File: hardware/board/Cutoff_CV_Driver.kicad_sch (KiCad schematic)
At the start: 18 parts

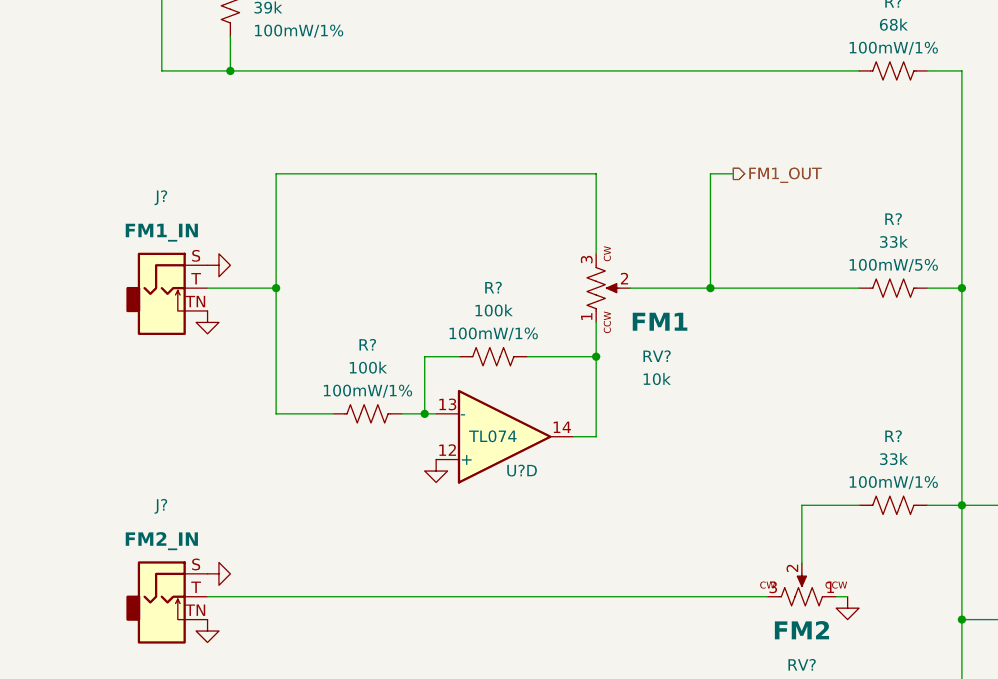
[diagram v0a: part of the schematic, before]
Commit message: Updated Schematic
-Added R935, R936, and Q901 to make resonance self oscillation LED turn on sharply

-Moved D929, D930, and added R933, R934 to make FM1 LED more sensitive

-Changed FM1 Attenuverter and added R410 and R411 to make FM1 Knob have some curve/deadzone

-Changed Resonance VCA output and added R623 and R624 to make resonance VCA output higher voltage to avoid opamp offset being significant .

-Added testing documents
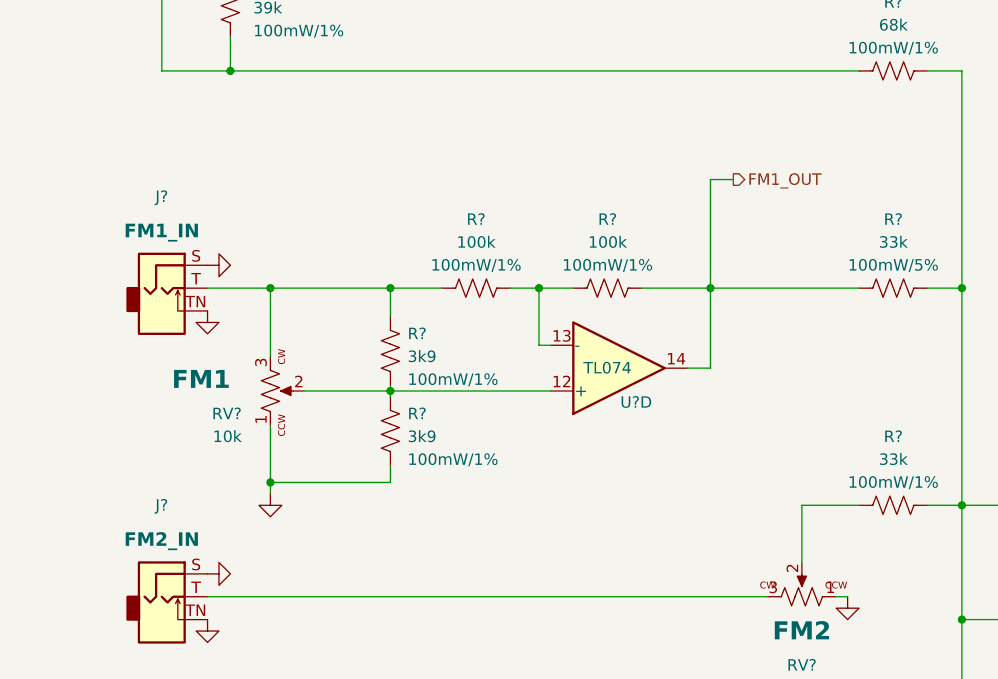
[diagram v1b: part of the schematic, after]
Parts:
- added R? (x2): 3k9, winterbloom:R_0603_HandSolder, symbol Device:R_US
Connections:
- net FM1_OUT: now also R?.1, U?.14; no longer RV?.2
- net GND: now also RV?.1, R?.2; no longer U?.12 (+)
- net at J?.T (Tip), R?.2, RV?.3: now also R?.1
- new net: R?.1, R?.2, RV?.2, U?.12 (+)
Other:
- moved on the sheet: R?, RV?, U?D

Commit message: Updated PCB to add and routed new components.
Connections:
- net INSTABILITY_IN renamed SALT_IN
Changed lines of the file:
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@@
   (title_block
     (title "Neptune")
-    (date "2023-07-20")
+    (date "2023-09-26")
     (rev "v0")
     (company "Winterbloom")
@@
     (effects (font (size 1.27 1.27)) (justify left))
   )
-  (hierarchical_label "INSTABILITY_IN" (shape input) (at 104.14 152.4 180) (fields_autoplaced)
+  (hierarchical_label "SALT_IN" (shape input) (at 104.14 152.4 180) (fields_autoplaced)
     (effects (font (size 1.27 1.27)) (justify right))
   )

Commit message: Lots of various small changes after reviewing the checklist.
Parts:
- R?: Rating 100mW/5% -> 100mW/1%
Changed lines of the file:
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@@
   (title_block
     (title "Neptune")
-    (date "2023-09-26")
-    (rev "v0")
+    (date "2023-10-10")
+    (rev "v1")
     (company "Winterbloom")
     (comment 1 "Carson Walls")
@@
       (effects (font (size 1.27 1.27)) hide)
     )
-    (property "Rating" "100mW/5%" (at 177.8 96.52 90)
-      (effects (font (size 1.27 1.27)))
-    )
+    (property "Rating" "100mW/1%" (at 177.8 96.52 90)
+      (effects (font (size 1.27 1.27)))
+    )

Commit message: hardware: add MPNs, DigiKey part numbers, and LCSC part numbers for all BOM items
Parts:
- C?: DigiKey (none) -> 1276-1008-1-ND; LCSC (none) -> C14858; MPN (none) -> CL10C101JB8NNNC; Rating 25V/10% -> 25V/10%/C0G; Substitutes Allowed (none) -> Yes
- R? (x2): DigiKey (none) -> 13-RT0603FRE13100KLTR-ND; LCSC (none) -> C4107493; MPN (none) -> RT0603FRE13100KL; Rating 100mW/1% -> 100mW/1%/Thin; Substitutes Allowed (none) -> Yes
- R? (x3): DigiKey (none) -> YAG5961CT-ND; LCSC (none) -> C863790; MPN (none) -> RT0603FRE073K9L; Rating 100mW/1% -> 100mW/1%/Thin; Substitutes Allowed (none) -> Yes
- R? (x2): DigiKey (none) -> YAG5967CT-ND; LCSC (none) -> C706189; MPN (none) -> RT0603FRE0768KL; Rating 100mW/1% -> 100mW/1%/Thin; Substitutes Allowed (none) -> Yes
- R?: DigiKey (none) -> YAG2321CT-ND; LCSC (none) -> C469659; MPN (none) -> RT0603FRE0710KL; Rating 100mW/1% -> 100mW/1%/Thin; Substitutes Allowed (none) -> Yes
- R? (x2): DigiKey (none) -> YAG5959CT-ND; LCSC (none) -> C706162; MPN (none) -> RT0603FRE0733KL; Rating 100mW/1% -> 100mW/1%/Thin; Substitutes Allowed (none) -> Yes
- R?: DigiKey (none) -> 13-RT0603FRE0739KLCT-ND; LCSC (none) -> C706166; MPN (none) -> RT0603FRE0739KL; Rating 100mW/1% -> 100mW/1%/Thin; Substitutes Allowed (none) -> Yes
- U? (x2): DigiKey (none) -> 296-7198-1-ND; LCSC (none) -> C96507; MPN TL074CPW -> TL074CPWR; Substitutes Allowed (none) -> No

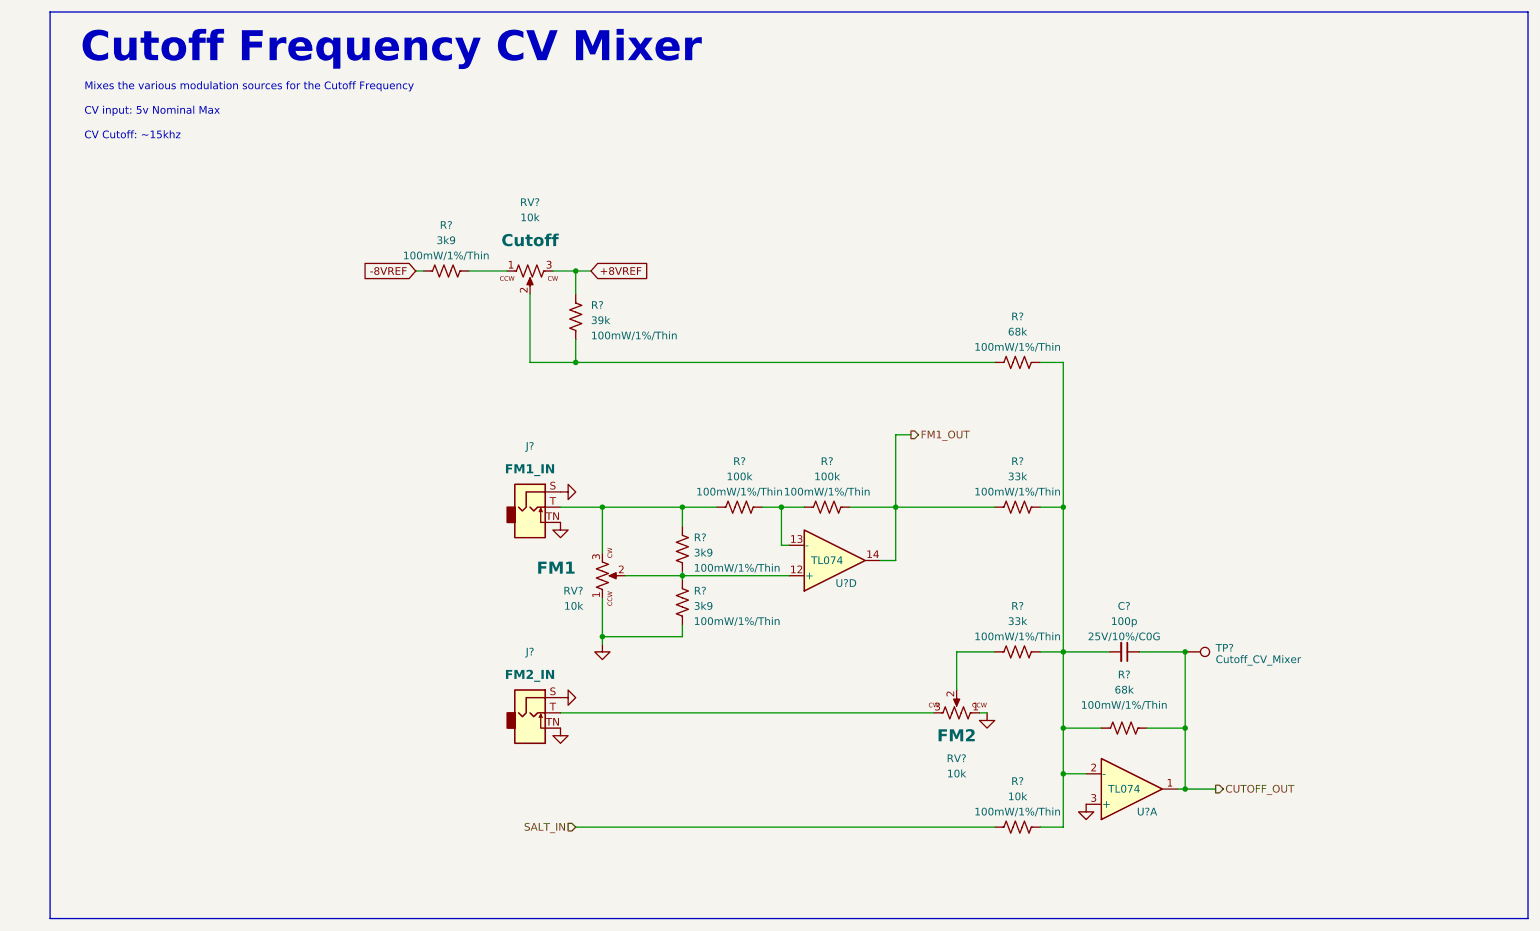
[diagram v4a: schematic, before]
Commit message: hardware: update schematic fonts/text sizes, some slight readability improvements
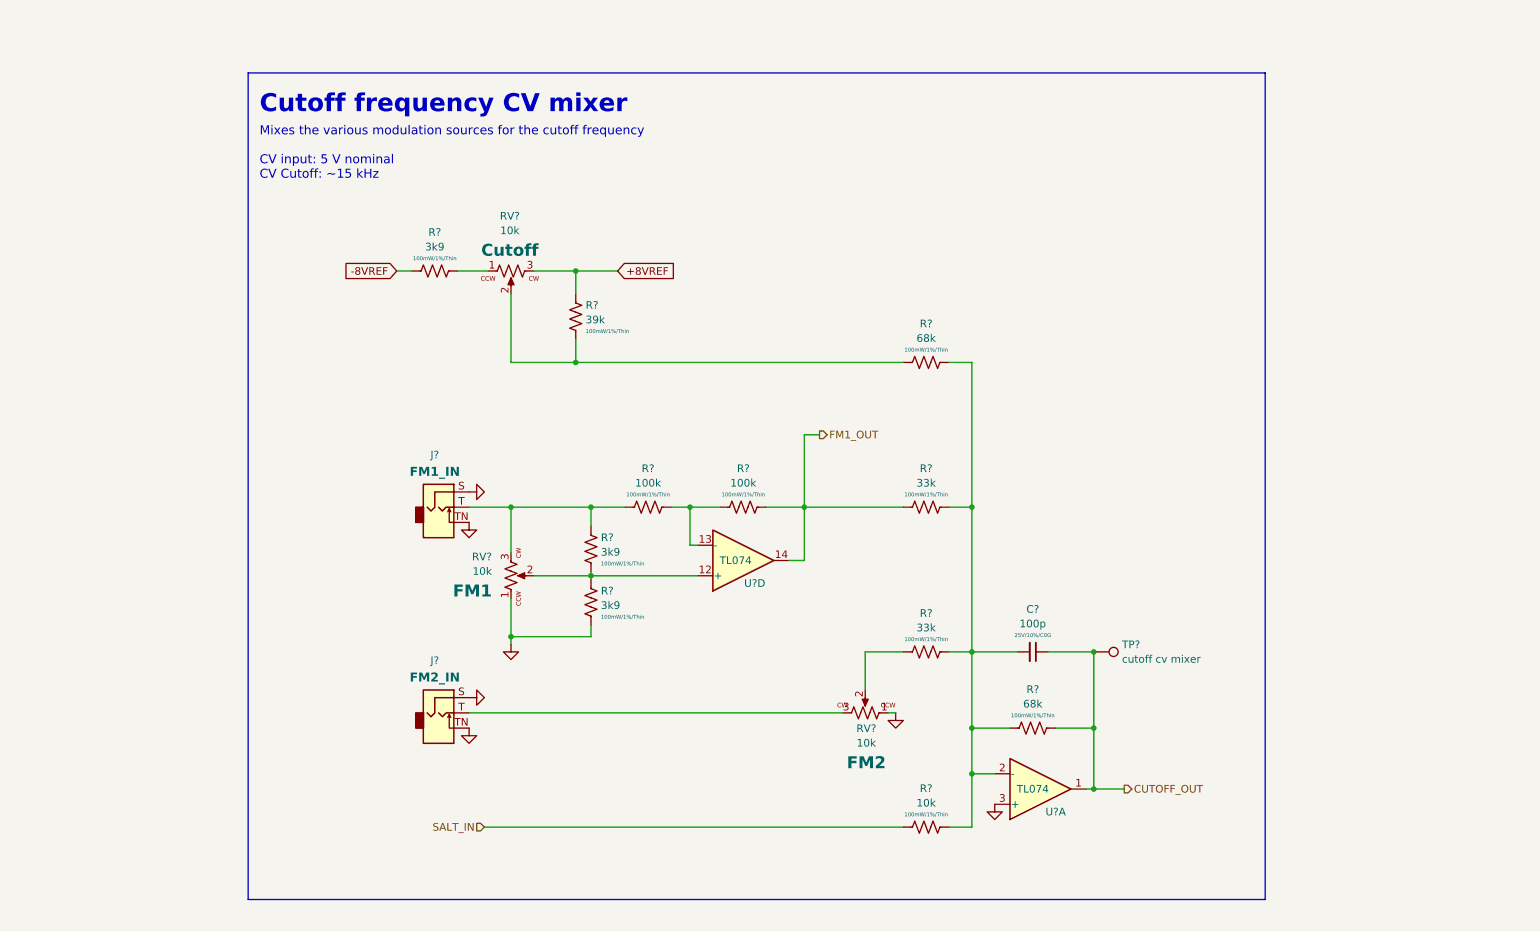
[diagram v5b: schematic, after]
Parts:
- TP?: Name Cutoff_CV_Mixer -> cutoff cv mixer
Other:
- note added: "Cutoff frequency CV mixer"
- note added: "Mixes the various modulation sources for the cutoff frequency CV input: 5 V nominal CV Cutoff: ~15 kHz"
- note removed: "Cutoff Frequency CV Mixer"
- note removed: "Mixes the various modulation sources for the Cutoff Frequency CV input: 5v Nominal Max CV Cutoff: ~15khz"
- moved on the sheet: C?, J?, R?, RV?, TP?, U?A, U?D

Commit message: hardware: use new Winterbloom sheet layout
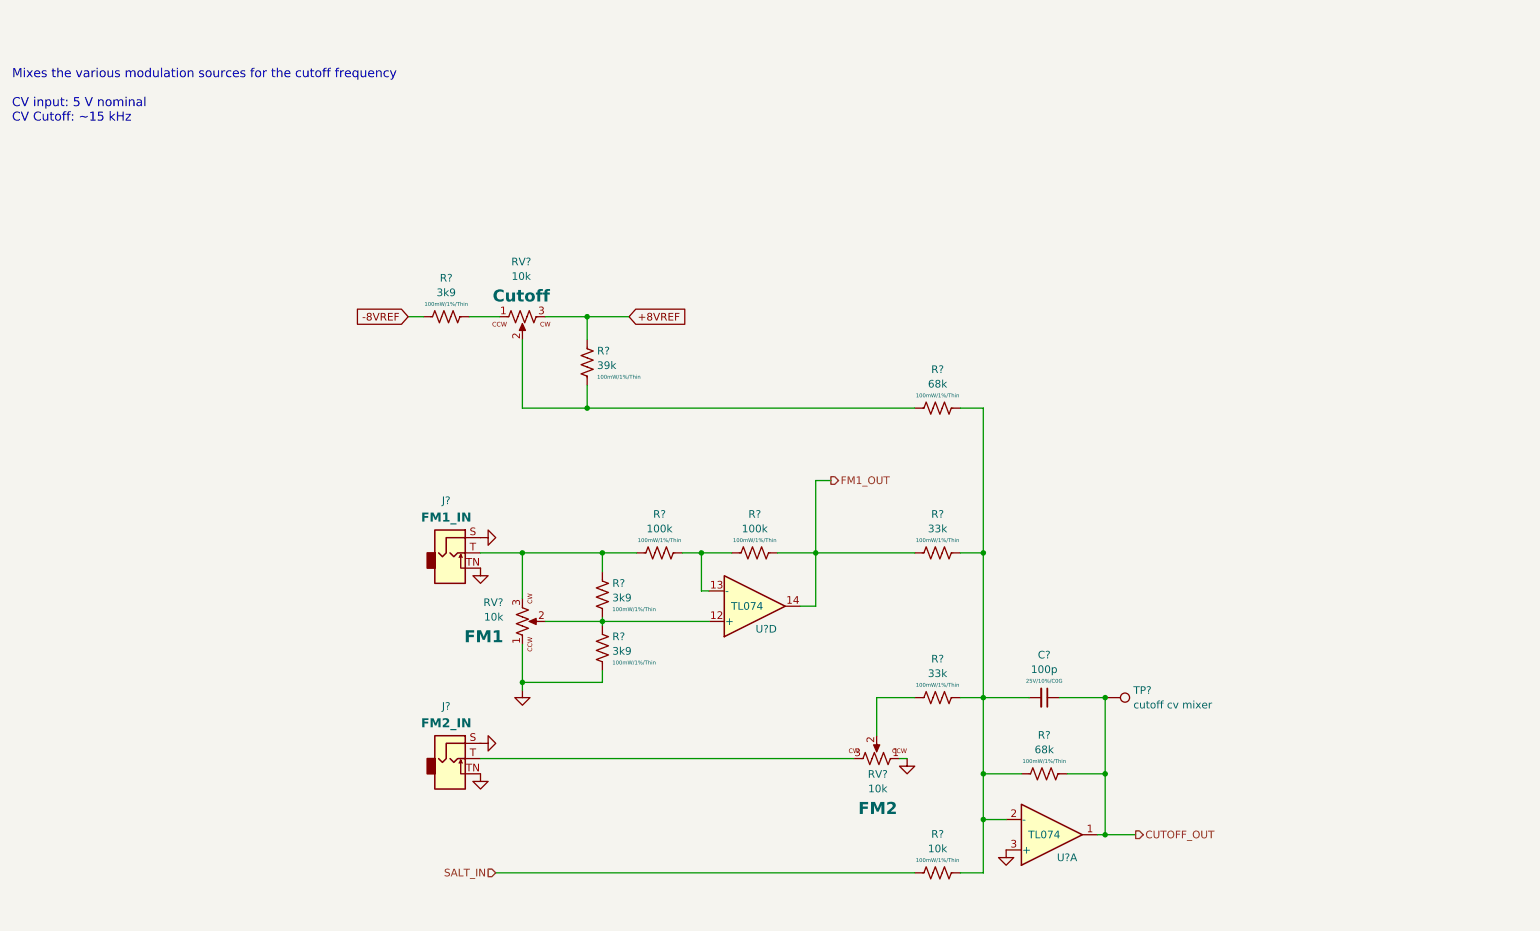
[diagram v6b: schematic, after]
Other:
- note removed: "Cutoff frequency CV mixer"
- moved on the sheet: C?, J?, R?, RV?, TP?, U?A, U?D

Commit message: hardware: finalize v3
- Updated version number and release date
- Swapped TL074C to TL074H
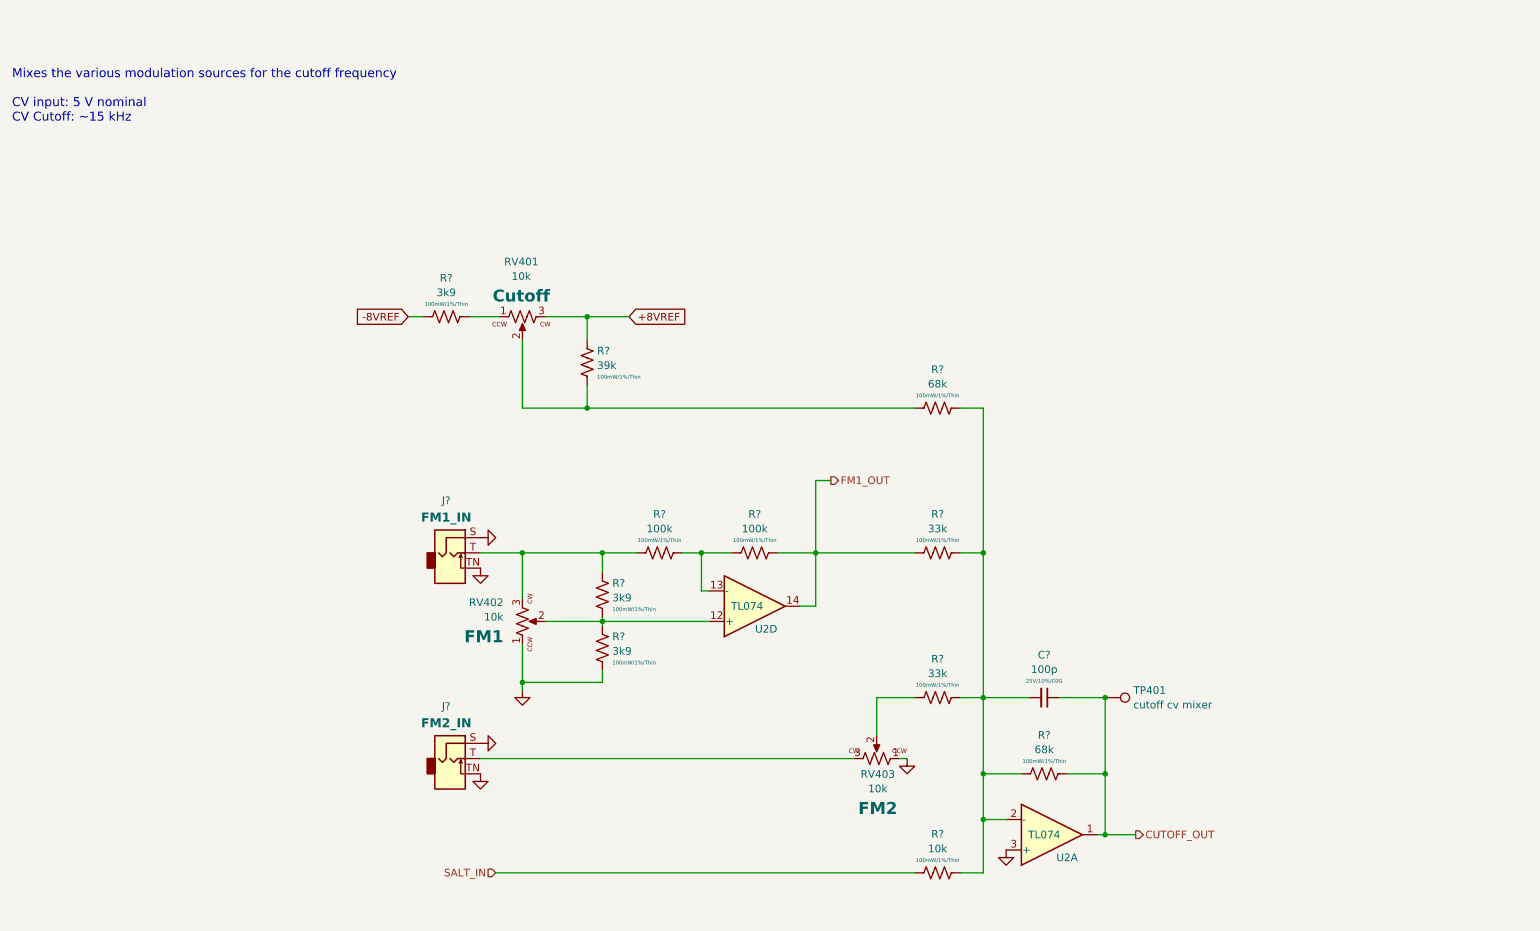
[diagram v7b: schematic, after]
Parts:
- U2: renamed from U?; DigiKey 296-7198-1-ND -> 296-TL074HIPWRCT-ND; LCSC C96507 -> C4370424; MPN TL074CPWR -> TL074HIPWR; Notes (none) -> TL074H over TL074C due to better input offset voltage
- gave numbers to parts that had none: 4
